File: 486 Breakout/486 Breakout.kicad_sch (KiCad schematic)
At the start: 36 parts, among them J1 PWR, J10 Conn_02x03_Counter_Clockwise, J11 Byte Enabled, J12 FPU, J13 Input, J14 Bus Size, J15 Bus Arbitration, J2 Conn_02x04_Counter_Clockwise, J3 Not Connected, J4 Address Bus, J5 Data Bus, J6 Conn_02x03_Counter_Clockwise, J7 Control Bus, J8 Cache, J9 Parity

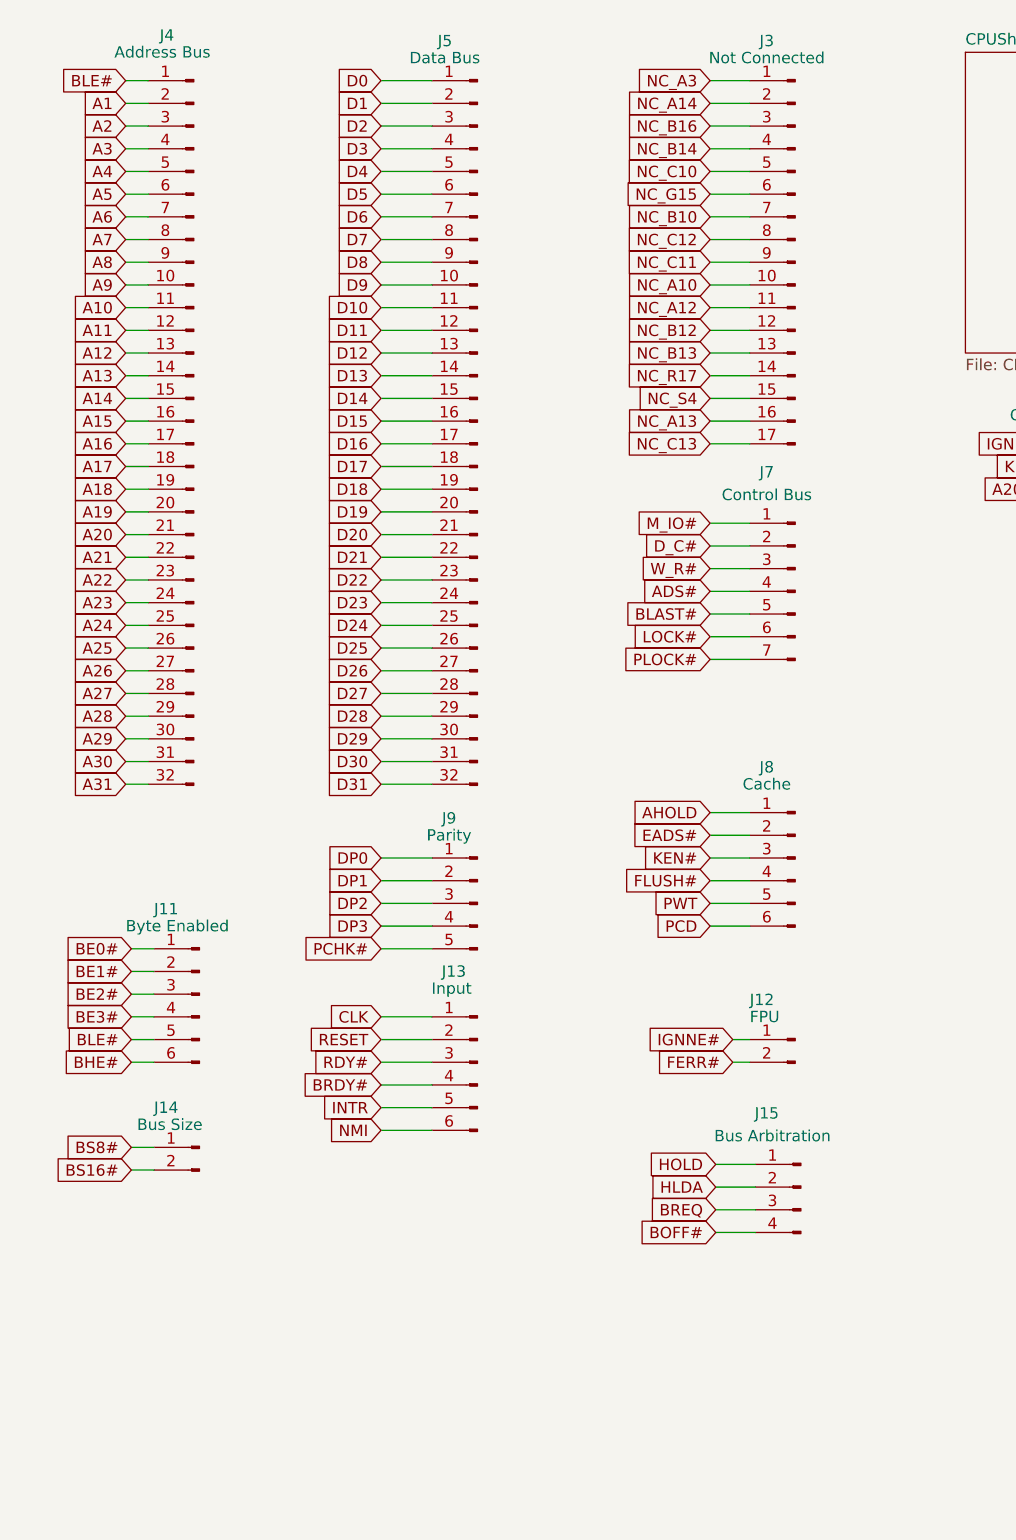
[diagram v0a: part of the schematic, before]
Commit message: * Updating  the 486 PCB * TestRom2 added
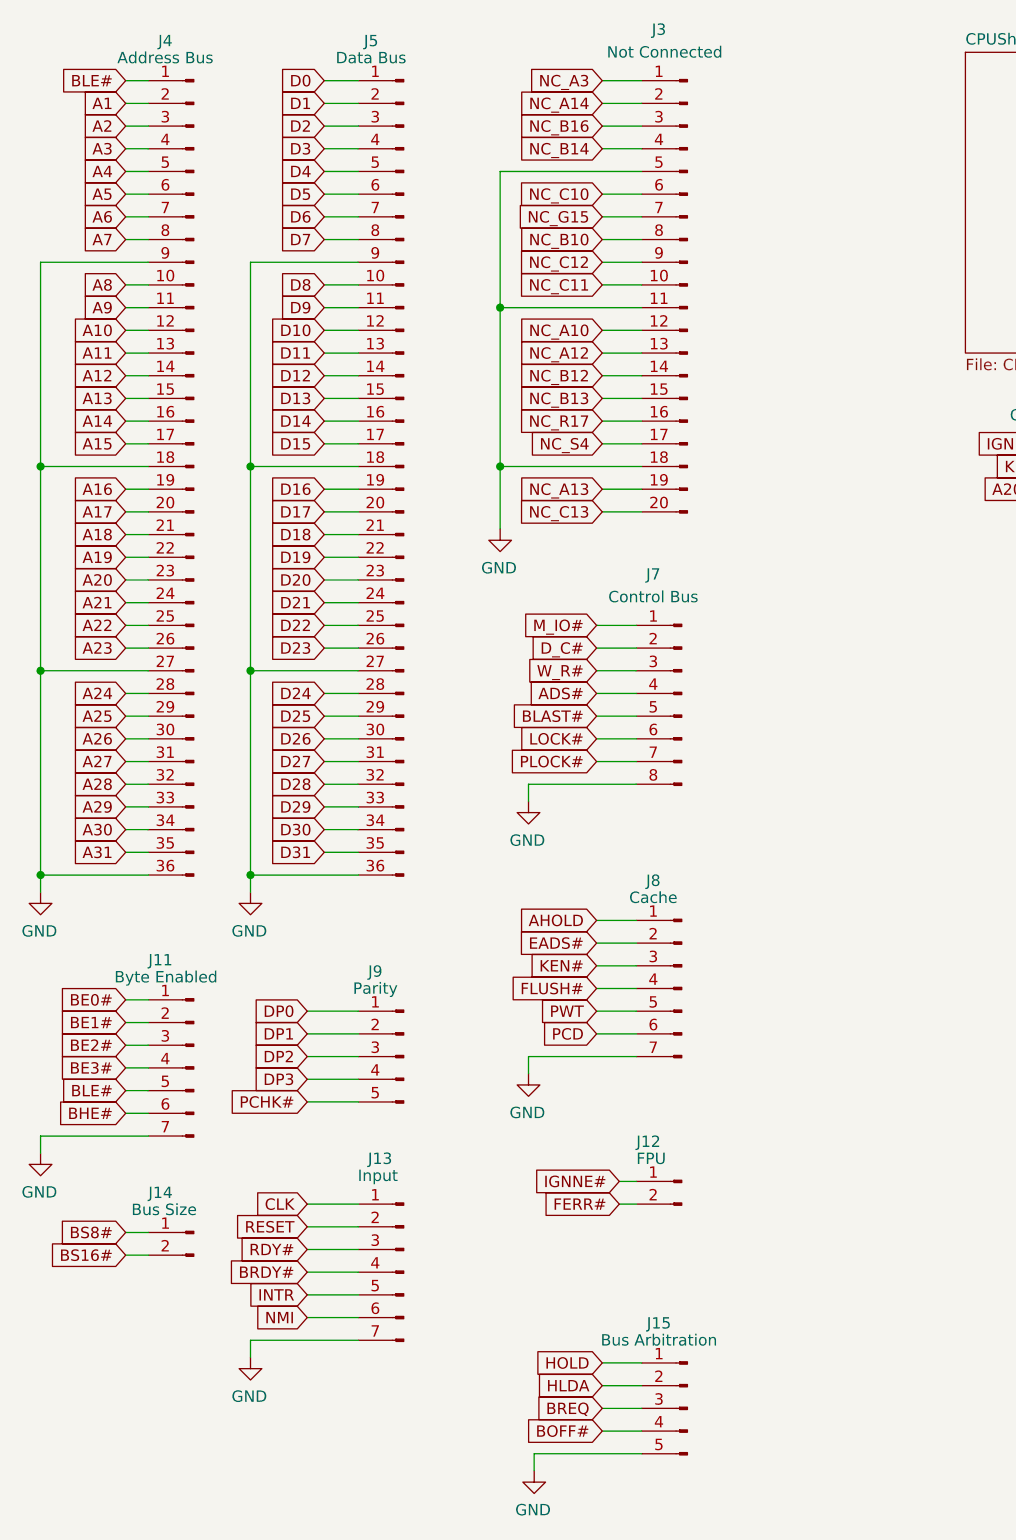
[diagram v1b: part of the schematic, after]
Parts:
- J11, J13, J8: footprint Connector_PinHeader_2.54mm:PinHeader_1x06_P2.54mm_Vertical -> Connector_PinHeader_2.54mm:PinHeader_1x07_P2.54mm_Vertical; symbol Connector:Conn_01x06_Male -> Connector:Conn_01x07_Male
- J15: footprint Connector_PinHeader_2.54mm:PinHeader_1x04_P2.54mm_Vertical -> Connector_PinHeader_2.54mm:PinHeader_1x05_P2.54mm_Vertical; symbol Connector:Conn_01x04_Male -> Connector:Conn_01x05_Male
- J3: footprint Connector_PinHeader_2.54mm:PinHeader_1x17_P2.54mm_Vertical -> Connector_PinHeader_2.54mm:PinHeader_1x20_P2.54mm_Vertical; symbol Connector:Conn_01x17_Male -> Connector:Conn_01x20_Male
- J4, J5: footprint Connector_PinHeader_2.54mm:PinHeader_1x32_P2.54mm_Vertical -> Connector_PinHeader_2.54mm:PinHeader_1x36_P2.54mm_Vertical; symbol Connector:Conn_01x32_Male -> Connector:Conn_01x36_Male
- J7: footprint Connector_PinHeader_2.54mm:PinHeader_1x07_P2.54mm_Vertical -> Connector_PinHeader_2.54mm:PinHeader_1x08_P2.54mm_Vertical; symbol Connector:Conn_01x07_Male -> Connector:Conn_01x08_Male
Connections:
- net A10: now also J4.12 (Pin_12); no longer J4.11 (Pin_11)
- net A11: now also J4.13 (Pin_13); no longer J4.12 (Pin_12)
- net A12: now also J4.14 (Pin_14); no longer J4.13 (Pin_13)
- net A13: now also J4.15 (Pin_15); no longer J4.14 (Pin_14)
- net A14: now also J4.16 (Pin_16); no longer J4.15 (Pin_15)
- net A15: now also J4.17 (Pin_17); no longer J4.16 (Pin_16)
- net A16: now also J4.19 (Pin_19); no longer J4.17 (Pin_17)
- net A17: now also J4.20 (Pin_20); no longer J4.18 (Pin_18)
- net A18: now also J4.21 (Pin_21); no longer J4.19 (Pin_19)
- net A19: now also J4.22 (Pin_22); no longer J4.20 (Pin_20)
- net A20: now also J4.23 (Pin_23); no longer J4.21 (Pin_21)
- net A21: now also J4.24 (Pin_24); no longer J4.22 (Pin_22)
- net A22: now also J4.25 (Pin_25); no longer J4.23 (Pin_23)
- net A23: now also J4.26 (Pin_26); no longer J4.24 (Pin_24)
- net A24: now also J4.28 (Pin_28); no longer J4.25 (Pin_25)
- net A25: now also J4.29 (Pin_29); no longer J4.26 (Pin_26)
- net A26: now also J4.30 (Pin_30); no longer J4.27 (Pin_27)
- net A27: now also J4.31 (Pin_31); no longer J4.28 (Pin_28)
- net A28: now also J4.32 (Pin_32); no longer J4.29 (Pin_29)
- net A29: now also J4.33 (Pin_33); no longer J4.30 (Pin_30)
- net A30: now also J4.34 (Pin_34); no longer J4.31 (Pin_31)
- net A31: now also J4.35 (Pin_35); no longer J4.32 (Pin_32)
- net A8: now also J4.10 (Pin_10); no longer J4.9 (Pin_9)
- net A9: now also J4.11 (Pin_11); no longer J4.10 (Pin_10)
- net D10: now also J5.12 (Pin_12); no longer J5.11 (Pin_11)
- net D11: now also J5.13 (Pin_13); no longer J5.12 (Pin_12)
- net D12: now also J5.14 (Pin_14); no longer J5.13 (Pin_13)
- net D13: now also J5.15 (Pin_15); no longer J5.14 (Pin_14)
- net D14: now also J5.16 (Pin_16); no longer J5.15 (Pin_15)
- net D15: now also J5.17 (Pin_17); no longer J5.16 (Pin_16)
- net D16: now also J5.19 (Pin_19); no longer J5.17 (Pin_17)
- net D17: now also J5.20 (Pin_20); no longer J5.18 (Pin_18)
- net D18: now also J5.21 (Pin_21); no longer J5.19 (Pin_19)
- net D19: now also J5.22 (Pin_22); no longer J5.20 (Pin_20)
- net D20: now also J5.23 (Pin_23); no longer J5.21 (Pin_21)
- net D21: now also J5.24 (Pin_24); no longer J5.22 (Pin_22)
- net D22: now also J5.25 (Pin_25); no longer J5.23 (Pin_23)
- net D23: now also J5.26 (Pin_26); no longer J5.24 (Pin_24)
- net D24: now also J5.28 (Pin_28); no longer J5.25 (Pin_25)
- net D25: now also J5.29 (Pin_29); no longer J5.26 (Pin_26)
- net D26: now also J5.30 (Pin_30); no longer J5.27 (Pin_27)
- net D27: now also J5.31 (Pin_31); no longer J5.28 (Pin_28)
- net D28: now also J5.32 (Pin_32); no longer J5.29 (Pin_29)
- net D29: now also J5.33 (Pin_33); no longer J5.30 (Pin_30)
- net D30: now also J5.34 (Pin_34); no longer J5.31 (Pin_31)
- net D31: now also J5.35 (Pin_35); no longer J5.32 (Pin_32)
- net D8: now also J5.10 (Pin_10); no longer J5.9 (Pin_9)
- net D9: now also J5.11 (Pin_11); no longer J5.10 (Pin_10)
- net GND: now also J11.7 (Pin_7), J13.7 (Pin_7), J15.5 (Pin_5), J3.11 (Pin_11), J3.18 (Pin_18), J3.5 (Pin_5), J4.18 (Pin_18), J4.27 (Pin_27), J4.36 (Pin_36), J4.9 (Pin_9), J5.18 (Pin_18), J5.27 (Pin_27), J5.36 (Pin_36), J5.9 (Pin_9), J7.8 (Pin_8), J8.7 (Pin_7)
- net NC_A10: now also J3.12 (Pin_12); no longer J3.10 (Pin_10)
- net NC_A12: now also J3.13 (Pin_13); no longer J3.11 (Pin_11)
- net NC_A13: now also J3.19 (Pin_19); no longer J3.16 (Pin_16)
- net NC_B10: now also J3.8 (Pin_8); no longer J3.7 (Pin_7)
- net NC_B12: now also J3.14 (Pin_14); no longer J3.12 (Pin_12)
- net NC_B13: now also J3.15 (Pin_15); no longer J3.13 (Pin_13)
- net NC_C10: now also J3.6 (Pin_6); no longer J3.5 (Pin_5)
- net NC_C11: now also J3.10 (Pin_10); no longer J3.9 (Pin_9)
- net NC_C12: now also J3.9 (Pin_9); no longer J3.8 (Pin_8)
- net NC_C13: now also J3.20 (Pin_20); no longer J3.17 (Pin_17)
- net NC_G15: now also J3.7 (Pin_7); no longer J3.6 (Pin_6)
- net NC_R17: now also J3.16 (Pin_16); no longer J3.14 (Pin_14)
- net NC_S4: now also J3.17 (Pin_17); no longer J3.15 (Pin_15)
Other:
- moved on the sheet: J12, J14, J9
